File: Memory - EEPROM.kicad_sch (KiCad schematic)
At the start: 8 parts, among them U2 CAT24C256

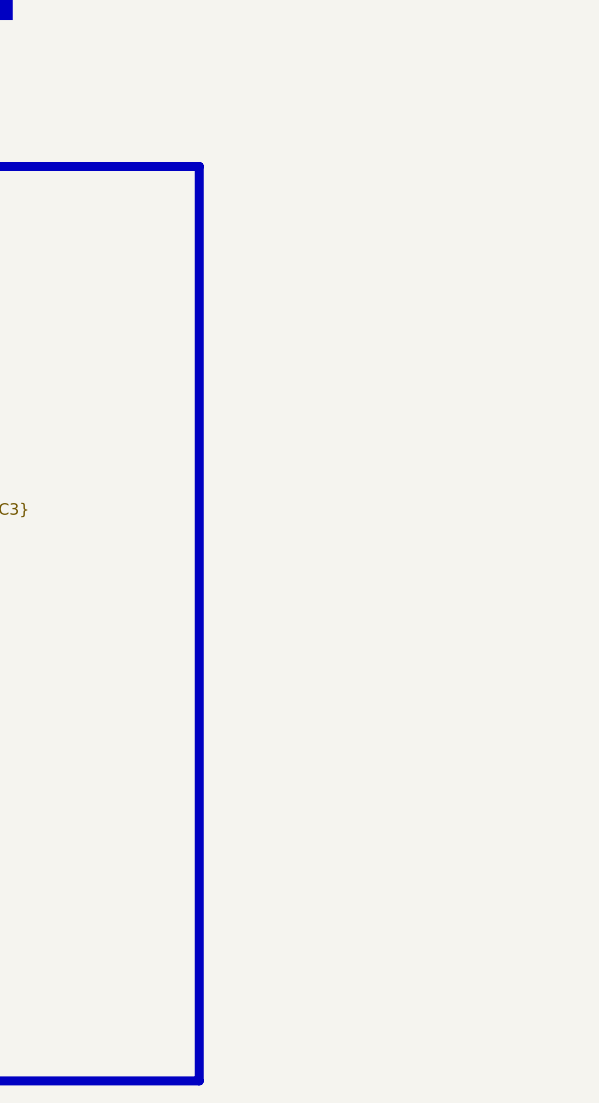
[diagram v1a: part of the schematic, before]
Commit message: added fiducal markers, mounting holes, testpoints
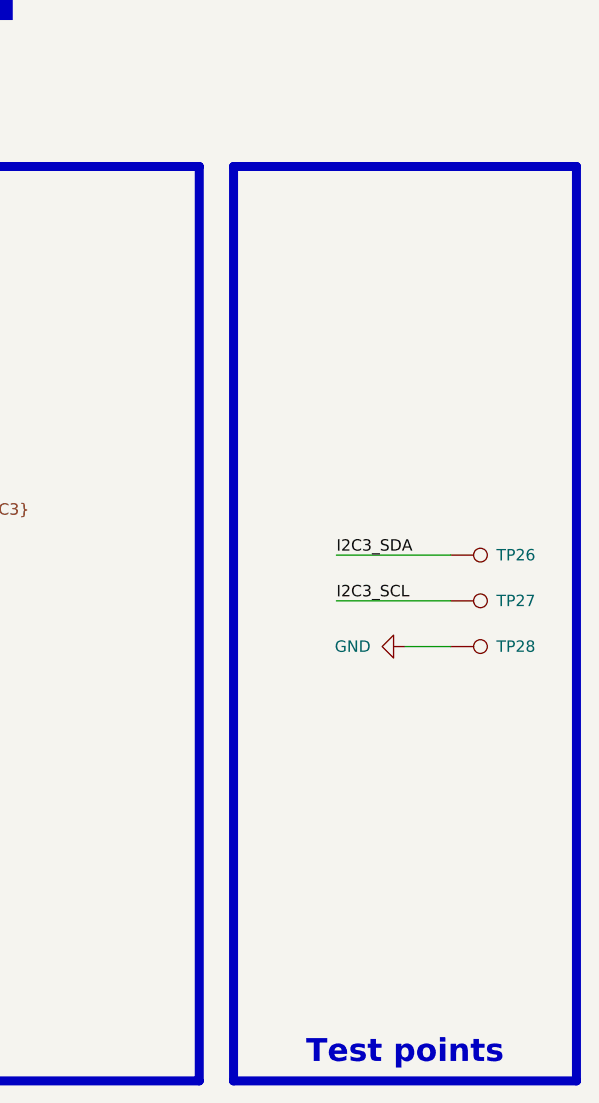
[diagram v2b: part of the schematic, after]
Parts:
- added TP26, TP27, TP28: TestPoint, 0_pads:TestPoint_Pad_D0.4mm_Back, symbol Connector:TestPoint
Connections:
- net GND: now also TP28.1
- net I2C3_SCL: now also TP27.1
- net I2C3_SDA: now also TP26.1

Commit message: test points, colors, drc
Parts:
- TP26, TP27, TP28: footprint 0_pads:TestPoint_Pad_D0.4mm_Back -> 0_pads:TestPoint_Pad_D0.5mm_Back
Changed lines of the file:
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@@
 			)
 		)
-		(property "Footprint" "0_pads:TestPoint_Pad_D0.4mm_Back"
+		(property "Footprint" "0_pads:TestPoint_Pad_D0.5mm_Back"
 			(at 256.54 86.36 0)
 			(effects
@@
 			)
 		)
-		(property "Footprint" "0_pads:TestPoint_Pad_D0.4mm_Back"
+		(property "Footprint" "0_pads:TestPoint_Pad_D0.5mm_Back"
 			(at 256.54 91.44 0)
 			(effects
@@
 			)
 		)
-		(property "Footprint" "0_pads:TestPoint_Pad_D0.4mm_Back"
+		(property "Footprint" "0_pads:TestPoint_Pad_D0.5mm_Back"
 			(at 256.54 96.52 0)
 			(effects

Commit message: designator chagnes and cleanup silkscreen
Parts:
- C8: LCSC PN (none) -> C1525
- R1, R2, R3, R4: LCSC PN (none) -> C25744
- R5, R6: LCSC PN (none) -> C17168
- U2: LCSC PN (none) -> C6482
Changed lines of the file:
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@@
 			)
 		)
-		(property "Description" "Resistor, small symbol"
+		(property "Description" "50V ±100ppm/℃ ±1% 10kΩ 0402"
 			(at 151.13 90.17 0)
 			(effects
@@
 		)
 		(property "Supplier Part Number 1" "C25744"
+			(at 151.13 90.17 0)
+			(effects
+				(font
+					(size 1.27 1.27)
+				)
+				(hide yes)
+			)
+		)
+		(property "LCSC PN" "C25744"
 			(at 151.13 90.17 0)
 			(effects
@@
 			)
 		)
-		(property "Description" "Resistor, small symbol"
+		(property "Description" "50V ±100ppm/℃ ±1% 10kΩ 0402"
 			(at 115.57 90.17 0)
 			(effects
@@
 		)
 		(property "Supplier Part Number 1" "C25744"
+			(at 115.57 90.17 0)
+			(effects
+				(font
+					(size 1.27 1.27)
+				)
+				(hide yes)
+			)
+		)
+		(property "LCSC PN" "C25744"
 			(at 115.57 90.17 0)
 			(effects
@@
 			)
 		)
-		(property "Description" "Resistor, small symbol"
+		(property "Description" "50V ±800ppm/℃ ±1% 0Ω 0402"
 			(at 173.99 83.82 0)
 			(effects
@@
 		)
 		(property "Supplier Part Number 1" "C17168"
+			(at 173.99 83.82 0)
+			(effects
+				(font
+					(size 1.27 1.27)
+				)
+				(hide yes)
+			)
+		)
+		(property "LCSC PN" "C17168"
 			(at 173.99 83.82 0)
 			(effects
@@
 			)
 		)
-		(property "Description" "Resistor, small symbol"
+		(property "Description" "50V ±100ppm/℃ ±1% 10kΩ 0402"
 			(at 124.46 90.17 0)
 			(effects
@@
 		)
 		(property "Supplier Part Number 1" "C25744"
+			(at 124.46 90.17 0)
+			(effects
+				(font
+					(size 1.27 1.27)
+				)
+				(hide yes)
+			)
+		)
+		(property "LCSC PN" "C25744"
 			(at 124.46 90.17 0)
 			(effects
@@
 			)
 		)
+		(property "LCSC PN" "C1525"
+			(at 132.08 72.39 0)
+			(effects
+				(font
+					(size 1.27 1.27)
+				)
+				(hide yes)
+			)
+		)
 		(pin "1"
 		)
@@
 			)
 		)
-		(property "Description" "Resistor, small symbol"
+		(property "Description" "50V ±100ppm/℃ ±1% 10kΩ 0402"
 			(at 106.68 90.17 0)
 			(effects
@@
 		)
 		(property "Supplier Part Number 1" "C25744"
+			(at 106.68 90.17 0)
+			(effects
+				(font
+					(size 1.27 1.27)
+				)
+				(hide yes)
+			)
+		)
+		(property "LCSC PN" "C25744"
 			(at 106.68 90.17 0)
 			(effects
@@
 			)
 		)
-		(property "Description" "Resistor, small symbol"
+		(property "Description" "50V ±800ppm/℃ ±1% 0Ω 0402"
 			(at 168.91 81.28 0)
 			(effects
@@
 		)
 		(property "Supplier Part Number 1" "C17168"
+			(at 168.91 81.28 0)
+			(effects
+				(font
+					(size 1.27 1.27)
+				)
+				(hide yes)
+			)
+		)
+		(property "LCSC PN" "C17168"
 			(at 168.91 81.28 0)
 			(effects
@@
 			(at 137.16 83.82 0)
 			(effects
+				(font
+					(size 1.27 1.27)
+				)
+				(hide yes)
+			)
+		)
+		(property "LCSC PN" "C6482"
+			(at 137.16 83.82 0)
+			(effects
